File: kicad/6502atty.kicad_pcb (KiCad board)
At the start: 2 copper layers, 104.9 x 113.3 mm, 102 parts, among them J1 Conn_01x04_Pin, J10 Conn_01x04_Pin, J11 Conn_01x03_Pin, J12 Conn_01x02_Pin, J2 Conn_01x02_Pin, J3 Conn_02x03_Odd_Even, J4 Conn_01x03_Pin, J5 Conn_01x06_Pin, J6 Conn_01x04_Pin, J7 Conn_01x10_Pin, J8 Conn_01x03_Pin, J9 Conn_01x10_Pin, SW1 SW_Push, U1 ATmega164P-20P, U10 74LS08, U11 74LS138, U12 74LS574, U2 74LS112, U3 W65C02SxP, U4 74LS574, U5 74HC245, U6 27C128, U7 KM62256CLP, U8 74LS00, U9 74LS00, Y1 18.432MHz

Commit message: pcb: add option for radial instead of axial capacitors
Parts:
- added C25: 100uF/16V, Capacitor_THT:CP_Radial_D6.3mm_P2.50mm, F.Cu at (11.1, 46.5)
- added C26: 100uF/16V, Capacitor_THT:CP_Radial_D6.3mm_P2.50mm, F.Cu at (99.8, 36.3)
- added C27: 100uF/16V, Capacitor_THT:CP_Radial_D6.3mm_P2.50mm, F.Cu at (100.5, 93.9)

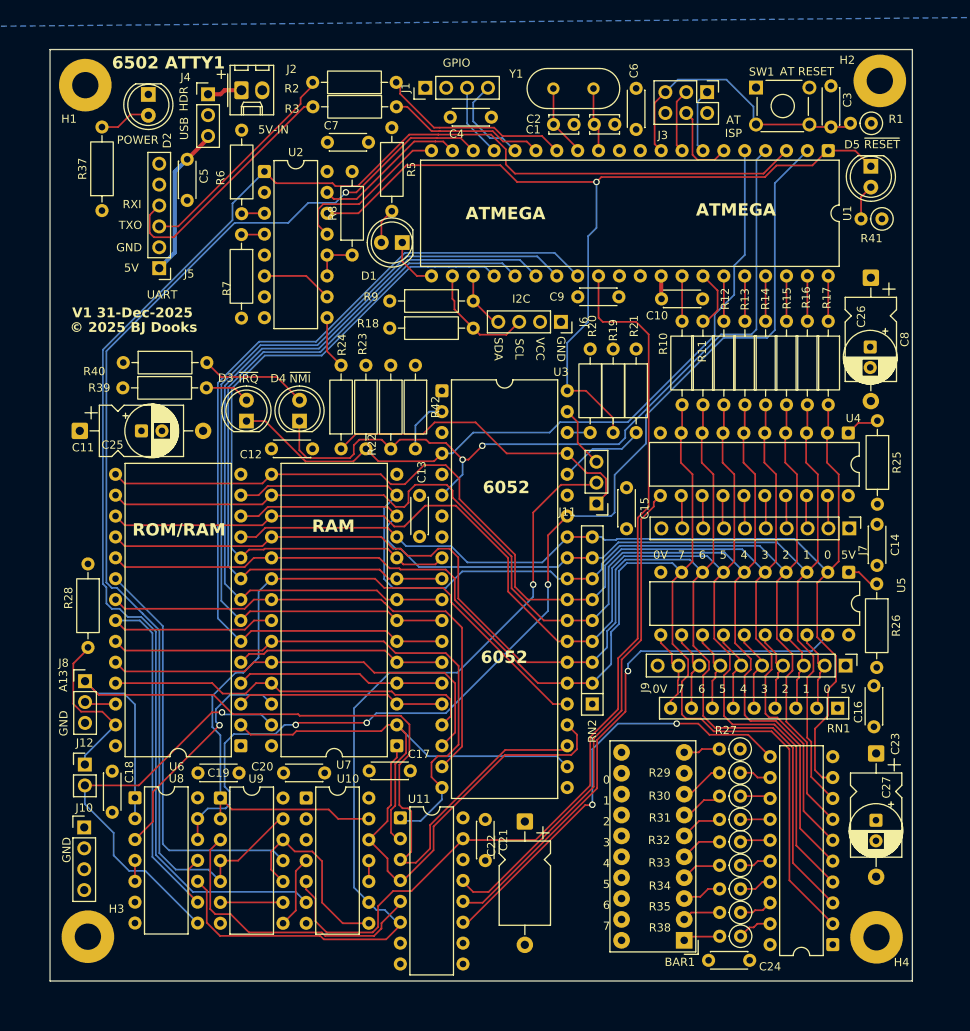
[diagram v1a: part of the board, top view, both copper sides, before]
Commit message: pcb: route tidying, reduce size, re-do teardrops
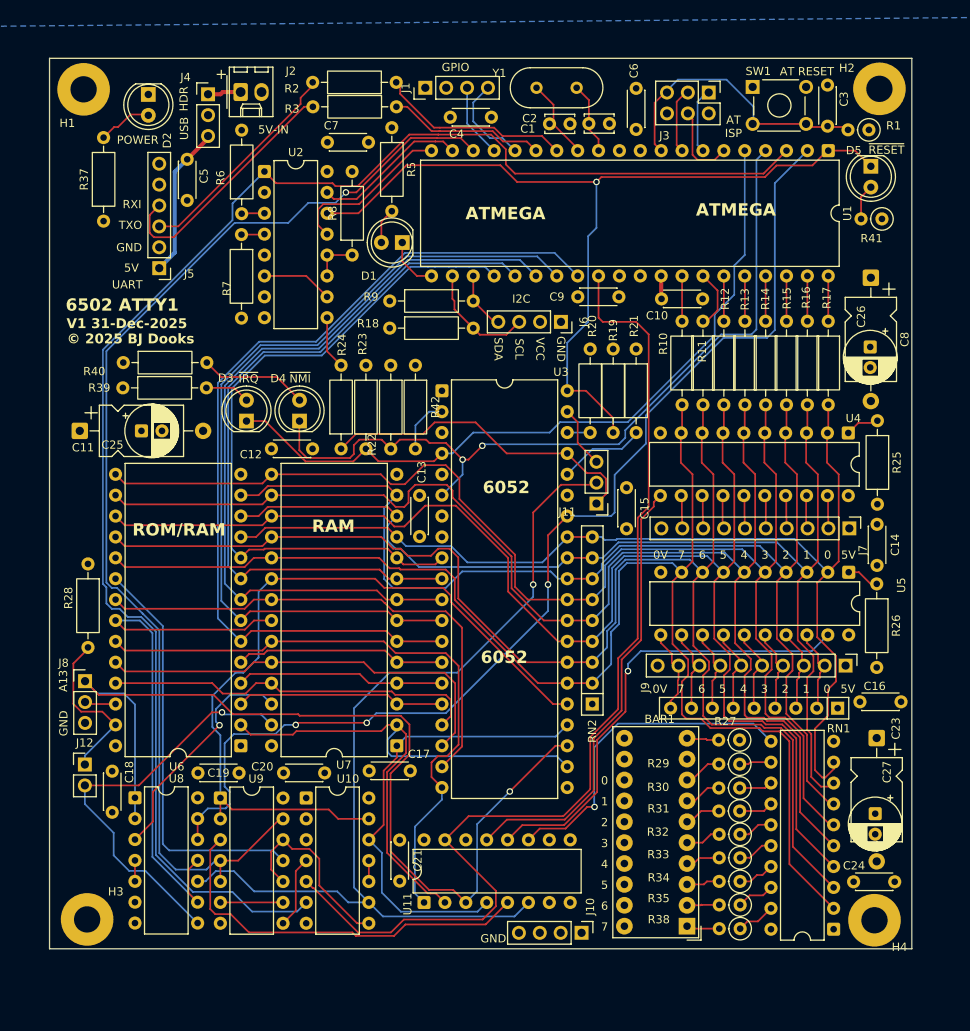
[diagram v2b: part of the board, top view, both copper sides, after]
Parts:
- removed C22: 100uF/16V, Capacitor_THT:CP_Axial_L10.0mm_D6.0mm_P15.00mm_Horizontal
- R1: value 1K -> 10K
- moved J10 61.8 mm to (64.6, 107.6), turned to -90 degrees
- moved C24 15.8 mm to (97.7, 101.4), turned to 0 degrees
- moved C21 10.7 mm to (42.5, 96.3)
- moved U11 10.7 mm to (45.5, 103.9), turned to 90 degrees
- moved C16 3.48 mm to (98.5, 79.5), turned to 0 degrees
- moved H3 2.10 mm to (4.50, 106.0)
- moved H4 2.09 mm to (100.3, 106.1)
- moved Y1 2.05 mm to (64.0, 4.80)
- moved U12 1.88 mm to (95.3, 107.2)
- moved C23 1.87 mm to (100.5, 83.9)
- moved BAR1 1.76 mm to (77.5, 106.8)
- moved R37 1.30 mm to (6.50, 21.0)
- moved R27 1.10 mm to (83.9, 84.1)
- moved R29 1.05 mm to (83.9, 87.1)
- moved R31 1.03 mm to (83.9, 92.8)
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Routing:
- net /A12: track 58.7 -> 72.8 mm
- net /~{DISPLAY}: track 53.4 -> 40.9 mm, vias 2 -> 1
- net /control/~{A15}: track 35.8 -> 48.1 mm
- net /AT_~{CE}: track 118.2 -> 128.1 mm
- net /~{IO_IN}: track 64.6 -> 56.2 mm
- net /A11: track 69.1 -> 77.0 mm
- net /PHI2: track 107.1 -> 115.0 mm
- net /A13: track 109.7 -> 116.6 mm, vias 0 -> 1
- net /~{IO_OUT}: track 60.6 -> 54.7 mm
- net /A14: track 54.2 -> 55.9 mm
- net /Atmel Controller/AT_XTI: track 8.78 -> 10.4 mm
- net /D2: track 139.9 -> 138.3 mm
- net /D0: track 127.2 -> 128.6 mm
- net Net-(BAR1H-A): track 5.96 -> 4.67 mm
- net /D7: track 168.8 -> 167.6 mm
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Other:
- board size 104.9 x 113.3 mm -> 104.9 x 108.3 mm

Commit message: pcb: minor updates to move stuff around
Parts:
- moved J12 2.12 mm to (4.76, 89.2)
- moved C16 1.45 mm to (98.3, 78.1)
- moved J8 0.75 mm to (4.98, 77.1)
- moved C18 0.43 mm to (7.90, 87.7)
- moved R28 0.24 mm to (4.83, 62.6)
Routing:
- net /D0: track 128.6 -> 124.1 mm
- net /R~{W}ph: track 51.0 -> 49.0 mm
- net /A13: track 116.6 -> 115.0 mm
- net /D1: track 129.8 -> 128.2 mm
- net /~{ROM_PGM_WE}: track 20.2 -> 21.6 mm
- net /ROM_A13: track 3.81 -> 3.02 mm
